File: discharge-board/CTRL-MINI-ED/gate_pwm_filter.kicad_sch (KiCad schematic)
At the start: 4 parts

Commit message: Add netlist class
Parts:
- renumbered C1 to C38, L1 to L3, R8 to R32, R34 to R33
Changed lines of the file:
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@@
 		(on_board yes)
 		(dnp no)
-		(property "Reference" "R8"
+		(property "Reference" "R32"
 			(at 64.77 46.736 0)
 			(effects
@@
 			(project "CTRL-MINI-ED"
 				(path "/3fa1ca74-4d0d-40dd-8b5c-0d4be11bd5b5/427c9eb0-5bf5-4b7b-8ffc-9f840385400e"
-					(reference "R8")
+					(reference "R32")
 					(unit 1)
 				)
@@
 		(on_board yes)
 		(dnp no)
-		(property "Reference" "C1"
+		(property "Reference" "C38"
 			(at 78.74 57.912 0)
 			(effects
@@
 			(project "CTRL-MINI-ED"
 				(path "/3fa1ca74-4d0d-40dd-8b5c-0d4be11bd5b5/427c9eb0-5bf5-4b7b-8ffc-9f840385400e"
-					(reference "C1")
+					(reference "C38")
 					(unit 1)
 				)
@@
 		(on_board yes)
 		(dnp no)
-		(property "Reference" "R34"
+		(property "Reference" "R33"
 			(at 65.532 61.214 0)
 			(effects
@@
 			(project "CTRL-MINI-ED"
 				(path "/3fa1ca74-4d0d-40dd-8b5c-0d4be11bd5b5/427c9eb0-5bf5-4b7b-8ffc-9f840385400e"
-					(reference "R34")
+					(reference "R33")
 					(unit 1)
 				)
@@
 		(dnp no)
 		(fields_autoplaced yes)
-		(property "Reference" "L1"
+		(property "Reference" "L3"
 			(at 69.85 49.53 90)
 			(effects
@@
 			(project "CTRL-MINI-ED"
 				(path "/3fa1ca74-4d0d-40dd-8b5c-0d4be11bd5b5/427c9eb0-5bf5-4b7b-8ffc-9f840385400e"
-					(reference "L1")
+					(reference "L3")
 					(unit 1)
 				)
@@
 		(on_board yes)
 		(dnp no)
-		(property "Reference" "#PWR012"
+		(property "Reference" "#PWR052"
 			(at 62.23 71.12 0)
 			(effects
@@
 			(project "CTRL-MINI-ED"
 				(path "/3fa1ca74-4d0d-40dd-8b5c-0d4be11bd5b5/427c9eb0-5bf5-4b7b-8ffc-9f840385400e"
-					(reference "#PWR012")
+					(reference "#PWR052")
 					(unit 1)
 				)
@@
 		(on_board yes)
 		(dnp no)
-		(property "Reference" "#PWR058"
+		(property "Reference" "#PWR053"
 			(at 76.2 71.12 0)
 			(effects
@@
 			(project "CTRL-MINI-ED"
 				(path "/3fa1ca74-4d0d-40dd-8b5c-0d4be11bd5b5/427c9eb0-5bf5-4b7b-8ffc-9f840385400e"
-					(reference "#PWR058")
+					(reference "#PWR053")
 					(unit 1)
 				)

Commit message: Draft of PCB layout
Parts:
- added TP51: TestPoint, TestPoint:TestPoint_Pad_D1.5mm, symbol Connector:TestPoint
- renumbered R32 to R26, R33 to R27
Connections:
- net at L3.1, R26.2, R27.1: now also TP51.1
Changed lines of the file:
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@@
+	(wire
+		(pts
+			(xy 55.88 54.61) (xy 62.23 54.61)
+		)
+		(stroke
+			(width 0)
+			(type default)
+		)
+	)
 	(wire
 		(pts
@@
 		(on_board yes)
 		(dnp no)
-		(property "Reference" "R32"
+		(property "Reference" "R26"
 			(at 64.77 46.736 0)
 			(effects
@@
 			(project "CTRL-MINI-ED"
 				(path "/3fa1ca74-4d0d-40dd-8b5c-0d4be11bd5b5/427c9eb0-5bf5-4b7b-8ffc-9f840385400e"
-					(reference "R32")
+					(reference "R26")
 					(unit 1)
 				)
@@
 		(on_board yes)
 		(dnp no)
-		(property "Reference" "R33"
+		(property "Reference" "R27"
 			(at 65.532 61.214 0)
 			(effects
@@
 			(project "CTRL-MINI-ED"
 				(path "/3fa1ca74-4d0d-40dd-8b5c-0d4be11bd5b5/427c9eb0-5bf5-4b7b-8ffc-9f840385400e"
-					(reference "R33")
+					(reference "R27")
 					(unit 1)
 				)
@@
 		(on_board yes)
 		(dnp no)
-		(property "Reference" "#PWR052"
+		(property "Reference" "#PWR047"
 			(at 62.23 71.12 0)
 			(effects
@@
 			(project "CTRL-MINI-ED"
 				(path "/3fa1ca74-4d0d-40dd-8b5c-0d4be11bd5b5/427c9eb0-5bf5-4b7b-8ffc-9f840385400e"
-					(reference "#PWR052")
+					(reference "#PWR047")
+					(unit 1)
+				)
+			)
+		)
+	)
+	(symbol
+		(lib_id "Connector:TestPoint")
+		(at 55.88 54.61 0)
+		(unit 1)
+		(exclude_from_sim no)
+		(in_bom yes)
+		(on_board yes)
+		(dnp no)
+		(property "Reference" "TP51"
+			(at 54.102 49.276 0)
+			(effects
+				(font
+					(size 1.27 1.27)
+				)
+				(justify left)
+			)
+		)
+		(property "Value" "TestPoint"
+			(at 58.42 52.5779 0)
+			(effects
+				(font
+					(size 1.27 1.27)
+				)
+				(justify left)
+				(hide yes)
+			)
+		)
+		(property "Footprint" "TestPoint:TestPoint_Pad_D1.5mm"
+			(at 60.96 54.61 0)
+			(effects
+				(font
+					(size 1.27 1.27)
+				)
+				(hide yes)
+			)
+		)
+		(property "Datasheet" "~"
+			(at 60.96 54.61 0)
+			(effects
+				(font
+					(size 1.27 1.27)
+				)
+				(hide yes)
+			)
+		)
+		(property "Description" "test point"
+			(at 55.88 54.61 0)
+			(effects
+				(font
+					(size 1.27 1.27)
+				)
+				(hide yes)
+			)
+		)
+		(pin "1"
+		)
+		(instances
+			(project "CTRL-MINI-ED"
+				(path "/3fa1ca74-4d0d-40dd-8b5c-0d4be11bd5b5/427c9eb0-5bf5-4b7b-8ffc-9f840385400e"
+					(reference "TP51")
 					(unit 1)
 				)
@@
 		(on_board yes)
 		(dnp no)
-		(property "Reference" "#PWR053"
+		(property "Reference" "#PWR048"
 			(at 76.2 71.12 0)
 			(effects
@@
 			(project "CTRL-MINI-ED"
 				(path "/3fa1ca74-4d0d-40dd-8b5c-0d4be11bd5b5/427c9eb0-5bf5-4b7b-8ffc-9f840385400e"
-					(reference "#PWR053")
+					(reference "#PWR048")
 					(unit 1)
 				)

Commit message: Cleanup old powers
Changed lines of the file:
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@@
 		(dnp no)
 		(property "Reference" "R26"
-			(at 64.77 46.736 0)
+			(at 65.532 46.736 0)
 			(effects
 				(font
@@
 		)
 		(property "Value" "470"
-			(at 65.278 48.768 0)
+			(at 65.532 48.768 0)
 			(effects
 				(font

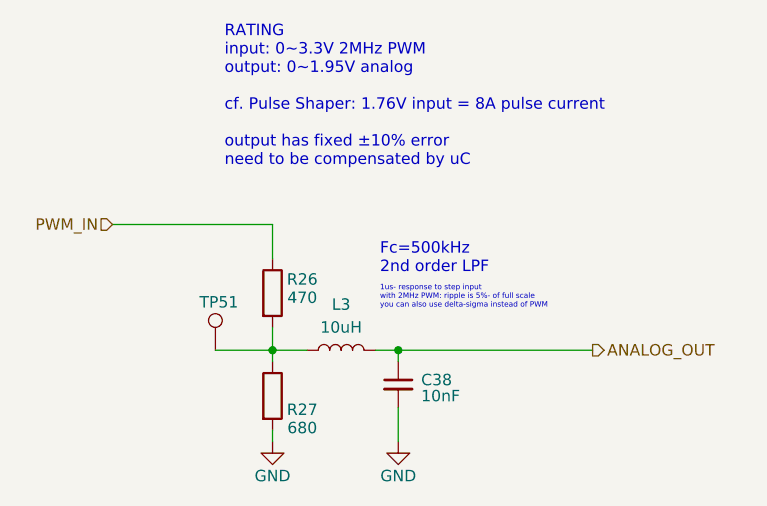
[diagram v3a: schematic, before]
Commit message: Basic building block layout
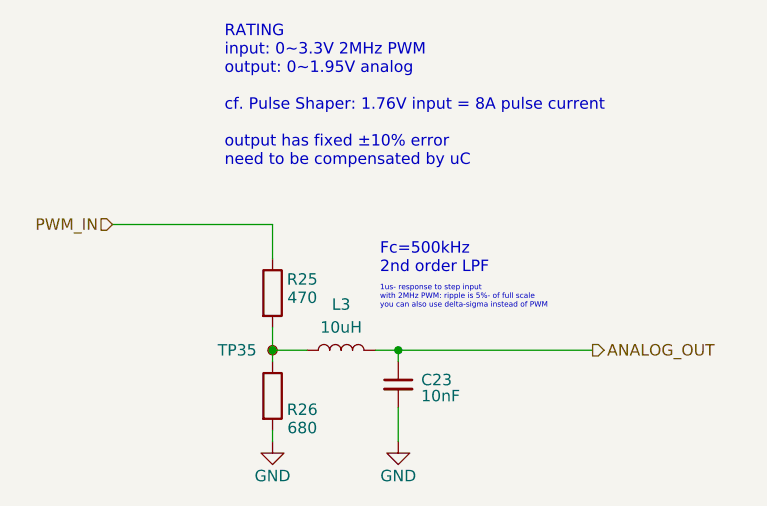
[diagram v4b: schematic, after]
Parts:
- TP35: renamed from TP51; symbol Connector:TestPoint -> Connector:TestPoint_Small
- renumbered C38 to C23, R26 to R25, R27 to R26
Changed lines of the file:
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@@
-	(wire
-		(pts
-			(xy 55.88 54.61) (xy 62.23 54.61)
-		)
-		(stroke
-			(width 0)
-			(type default)
-		)
-	)
 	(wire
 		(pts
@@
 		(on_board yes)
 		(dnp no)
-		(property "Reference" "R26"
+		(property "Reference" "R25"
 			(at 65.532 46.736 0)
 			(effects
@@
 			(project "CTRL-MINI-ED"
 				(path "/3fa1ca74-4d0d-40dd-8b5c-0d4be11bd5b5/427c9eb0-5bf5-4b7b-8ffc-9f840385400e"
-					(reference "R26")
+					(reference "R25")
 					(unit 1)
 				)
@@
 		(on_board yes)
 		(dnp no)
-		(property "Reference" "C38"
+		(property "Reference" "C23"
 			(at 78.74 57.912 0)
 			(effects
@@
 			(project "CTRL-MINI-ED"
 				(path "/3fa1ca74-4d0d-40dd-8b5c-0d4be11bd5b5/427c9eb0-5bf5-4b7b-8ffc-9f840385400e"
-					(reference "C38")
+					(reference "C23")
 					(unit 1)
 				)
@@
 		(on_board yes)
 		(dnp no)
-		(property "Reference" "R27"
+		(property "Reference" "R26"
 			(at 65.532 61.214 0)
 			(effects
@@
 			(project "CTRL-MINI-ED"
 				(path "/3fa1ca74-4d0d-40dd-8b5c-0d4be11bd5b5/427c9eb0-5bf5-4b7b-8ffc-9f840385400e"
-					(reference "R27")
+					(reference "R26")
 					(unit 1)
 				)
@@
 		(on_board yes)
 		(dnp no)
-		(property "Reference" "#PWR047"
+		(property "Reference" "#PWR033"
 			(at 62.23 71.12 0)
 			(effects
@@
 			(project "CTRL-MINI-ED"
 				(path "/3fa1ca74-4d0d-40dd-8b5c-0d4be11bd5b5/427c9eb0-5bf5-4b7b-8ffc-9f840385400e"
-					(reference "#PWR047")
+					(reference "#PWR033")
 					(unit 1)
 				)
@@
 	)
 	(symbol
-		(lib_id "Connector:TestPoint")
-		(at 55.88 54.61 0)
+		(lib_id "Connector:TestPoint_Small")
+		(at 62.23 54.61 0)
 		(unit 1)
 		(exclude_from_sim no)
@@
 		(on_board yes)
 		(dnp no)
-		(property "Reference" "TP51"
-			(at 54.102 49.276 0)
+		(property "Reference" "TP35"
+			(at 56.134 54.61 0)
 			(effects
 				(font
@@
 		)
 		(property "Value" "TestPoint"
-			(at 58.42 52.5779 0)
+			(at 64.77 52.5779 0)
 			(effects
 				(font
@@
 		)
 		(property "Footprint" "TestPoint:TestPoint_Pad_D1.5mm"
-			(at 60.96 54.61 0)
+			(at 67.31 54.61 0)
 			(effects
 				(font
@@
 		)
 		(property "Datasheet" "~"
-			(at 60.96 54.61 0)
+			(at 67.31 54.61 0)
 			(effects
 				(font
@@
 		)
 		(property "Description" "test point"
-			(at 55.88 54.61 0)
+			(at 62.23 54.61 0)
 			(effects
 				(font
@@
 			(project "CTRL-MINI-ED"
 				(path "/3fa1ca74-4d0d-40dd-8b5c-0d4be11bd5b5/427c9eb0-5bf5-4b7b-8ffc-9f840385400e"
-					(reference "TP51")
+					(reference "TP35")
 					(unit 1)
 				)
@@
 		(on_board yes)
 		(dnp no)
-		(property "Reference" "#PWR048"
+		(property "Reference" "#PWR034"
 			(at 76.2 71.12 0)
 			(effects
@@
 			(project "CTRL-MINI-ED"
 				(path "/3fa1ca74-4d0d-40dd-8b5c-0d4be11bd5b5/427c9eb0-5bf5-4b7b-8ffc-9f840385400e"
-					(reference "#PWR048")
+					(reference "#PWR034")
 					(unit 1)
 				)

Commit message: Fix wrong part & footprint assignment
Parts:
- R25: LCSC C21190 -> C23179
- R26: LCSC C21190 -> C23228
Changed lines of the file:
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@@
 			)
 		)
-		(property "LCSC" "C21190"
+		(property "LCSC" "C23179"
 			(at 62.23 48.26 0)
 			(effects
@@
 			)
 		)
-		(property "LCSC" "C21190"
+		(property "LCSC" "C23228"
 			(at 62.23 59.69 0)
 			(effects
